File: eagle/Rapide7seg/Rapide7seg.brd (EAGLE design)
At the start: 50 x 50 mm, 47 parts, among them IC1 MEGA8-P, J1 AVR_SPI_PRG_6PTH

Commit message: First version, sent to production
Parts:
- moved C3 0.90 mm to (1.91, 40.0), turned to 270 degrees
- moved LED4 0.64 mm to (40.0, 43.2)
- moved LED1 0.63 mm to (9.53, 43.2)
- moved H1 0.63 mm to (47.6, 47.0)
- moved LED2 0.63 mm to (19.7, 43.2)
- moved LED3 0.63 mm to (29.8, 43.2)
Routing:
- net UCRESET: track 0.00 -> 126.0 mm, vias 0 -> 3
- net GND: track 0.00 -> 125.9 mm, vias 0 -> 2
- net VCC: track 0.00 -> 114.2 mm, vias 0 -> 2
- net N$21: track 0.00 -> 86.4 mm, vias 0 -> 4
- net N$23: track 0.00 -> 86.3 mm, vias 0 -> 2
- net N$16: track 0.00 -> 63.2 mm, vias 0 -> 2
- net N$19: track 0.00 -> 61.6 mm, vias 0 -> 4
- net N$17: track 0.00 -> 60.3 mm, vias 0 -> 2
- net N$1: track 0.00 -> 59.8 mm
- net N$9: track 0.00 -> 55.0 mm
- net N$11: track 0.00 -> 50.0 mm
- net L3: track 0.00 -> 49.5 mm, vias 0 -> 2
- net N$26: track 0.00 -> 48.8 mm, vias 0 -> 1
- net L1: track 0.00 -> 48.4 mm, vias 0 -> 2
- net N$22: track 0.00 -> 48.0 mm, vias 0 -> 3
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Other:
- board text removed: "Order #######"

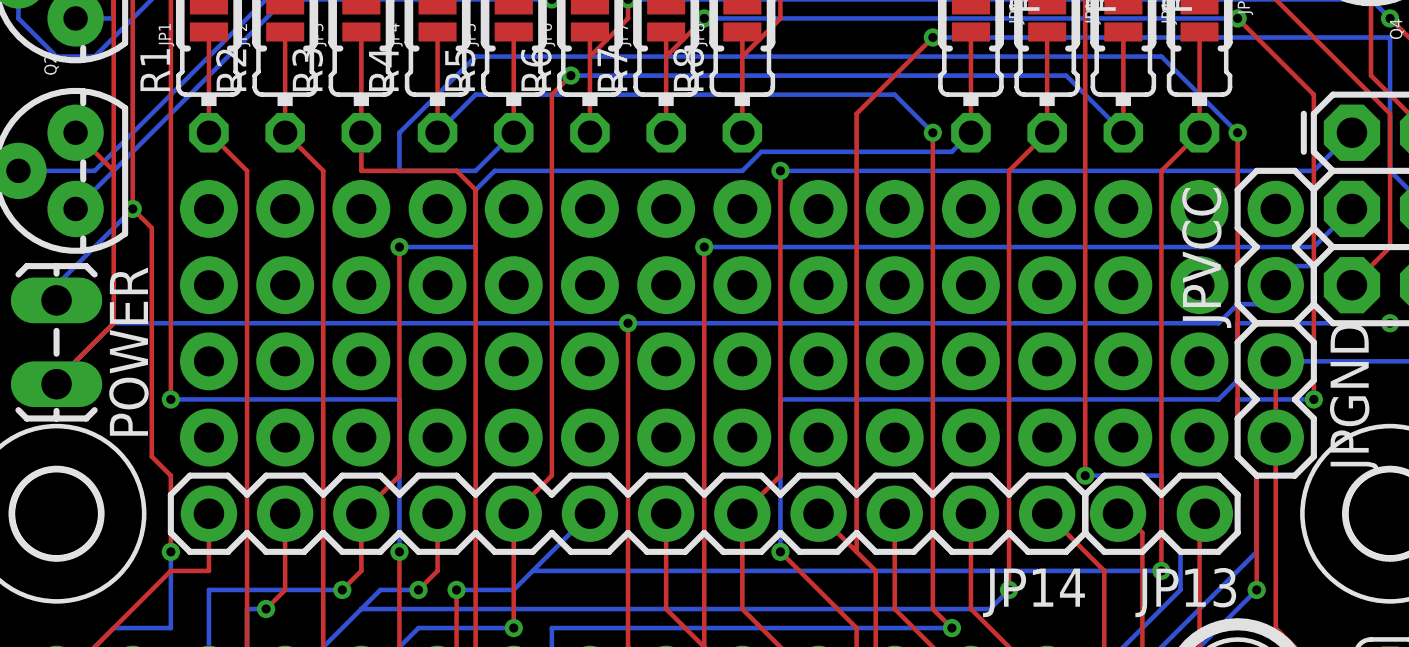
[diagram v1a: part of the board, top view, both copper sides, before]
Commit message: edit/bugfix (wrongly used vias instead of pins)
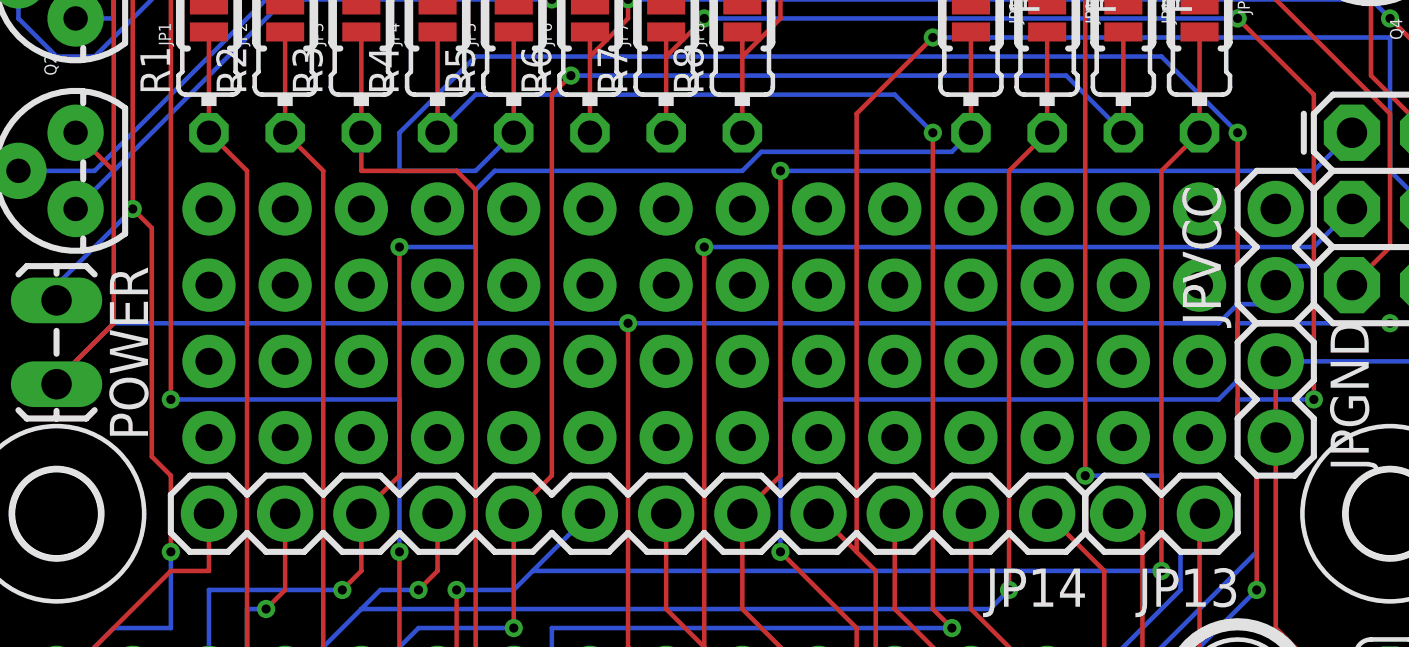
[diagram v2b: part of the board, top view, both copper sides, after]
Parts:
- added U$1, U$2, U$3, U$4, U$5, U$6, U$7, U$8: M7_NOSILK, kalshagar:M7_NOSILK
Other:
- board text added: "v1.1 Mar2013"
- board text removed: "v1.0 Nov2012"
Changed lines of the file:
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@@
 <layer number="144" name="Drill_legend" color="7" fill="1" visible="no" active="yes"/>
 <layer number="151" name="HeatSink" color="7" fill="1" visible="no" active="yes"/>
+<layer number="199" name="Contour" color="7" fill="1" visible="yes" active="yes"/>
 <layer number="200" name="200bmp" color="1" fill="10" visible="no" active="yes"/>
 <layer number="201" name="201bmp" color="2" fill="10" visible="no" active="yes"/>
@@
 <text x="24.13" y="6.35" size="1.4224" layer="125">Rapide7seg</text>
 <text x="6.35" y="3.81" size="1.016" layer="125">kalshagar.wikispaces.com/Rapide7seg</text>
-<text x="27.94" y="5.08" size="0.8128" layer="125">v1.0 Nov2012</text>
+<text x="27.94" y="5.08" size="0.8128" layer="125">v1.1 Mar2013</text>
 <wire x1="46.355" y1="17.78" x2="46.355" y2="20.32" width="0.254" layer="125"/>
 <wire x1="46.355" y1="20.32" x2="44.45" y2="20.32" width="0.254" layer="125"/>
@@
 <element name="JPVCC" library="SparkFun" package="1X02" value="" x="43.18" y="22.86" rot="R90"/>
 <element name="C3" library="resistor" package="E1,8-4" value="" x="1.905" y="40.005" rot="R270"/>
+<element name="U$1" library="kalshagar" package="M7_NOSILK" value="M7_NOSILK" x="7.62" y="17.78"/>
+<element name="U$2" library="kalshagar" package="M7_NOSILK" value="M7_NOSILK" x="25.4" y="17.78"/>
+<element name="U$3" library="kalshagar" package="M7_NOSILK" value="M7_NOSILK" x="7.62" y="20.32"/>
+<element name="U$4" library="kalshagar" package="M7_NOSILK" value="M7_NOSILK" x="25.4" y="20.32"/>
+<element name="U$5" library="kalshagar" package="M7_NOSILK" value="M7_NOSILK" x="7.62" y="22.86"/>
+<element name="U$6" library="kalshagar" package="M7_NOSILK" value="M7_NOSILK" x="25.4" y="22.86"/>
+<element name="U$7" library="kalshagar" package="M7_NOSILK" value="M7_NOSILK" x="7.62" y="25.4"/>
+<element name="U$8" library="kalshagar" package="M7_NOSILK" value="M7_NOSILK" x="25.4" y="25.4"/>
 </elements>
 <signals>
@@
 <wire x1="35.56" y1="15.24" x2="37.465" y2="13.335" width="0.1524" layer="1"/>
 </signal>
-<signal name="N$43">
-<via x="7.62" y="25.4" extent="1-16" drill="1" diameter="1.9304"/>
-</signal>
-<signal name="N$44">
-<via x="7.62" y="22.86" extent="1-16" drill="1" diameter="1.9304"/>
-</signal>
-<signal name="N$45">
-<via x="7.62" y="17.78" extent="1-16" drill="1" diameter="1.9304"/>
-</signal>
-<signal name="N$42">
-<via x="7.62" y="20.32" extent="1-16" drill="1" diameter="1.9304"/>
-</signal>
-<signal name="N$46">
-<via x="10.16" y="25.4" extent="1-16" drill="1" diameter="1.9304"/>
-</signal>
-<signal name="N$47">
-<via x="10.16" y="22.86" extent="1-16" drill="1" diameter="1.9304"/>
-</signal>
-<signal name="N$48">
-<via x="10.16" y="17.78" extent="1-16" drill="1" diameter="1.9304"/>
-</signal>
-<signal name="N$35">
-<via x="10.16" y="20.32" extent="1-16" drill="1" diameter="1.9304"/>
-</signal>
-<signal name="N$53">
-<via x="12.7" y="22.86" extent="1-16" drill="1" diameter="1.9304"/>
-</signal>
-<signal name="N$54">
-<via x="12.7" y="17.78" extent="1-16" drill="1" diameter="1.9304"/>
-</signal>
-<signal name="N$49">
-<via x="12.7" y="20.32" extent="1-16" drill="1" diameter="1.9304"/>
-</signal>
-<signal name="N$50">
-<via x="12.7" y="25.4" extent="1-16" drill="1" diameter="1.9304"/>
-</signal>
-<signal name="N$51">
-<via x="15.24" y="25.4" extent="1-16" drill="1" diameter="1.9304"/>
-</signal>
-<signal name="N$52">
-<via x="15.24" y="22.86" extent="1-16" drill="1" diameter="1.9304"/>
-</signal>
-<signal name="N$55">
-<via x="15.24" y="17.78" extent="1-16" drill="1" diameter="1.9304"/>
-</signal>
-<signal name="N$36">
-<via x="15.24" y="20.32" extent="1-16" drill="1" diameter="1.9304"/>
-</signal>
-<signal name="N$57">
-<via x="17.78" y="25.4" extent="1-16" drill="1" diameter="1.9304"/>
-</signal>
-<signal name="N$60">
-<via x="17.78" y="22.86" extent="1-16" drill="1" diameter="1.9304"/>
-</signal>
-<signal name="N$61">
-<via x="17.78" y="17.78" extent="1-16" drill="1" diameter="1.9304"/>
-</signal>
-<signal name="N$56">
-<via x="17.78" y="20.32" extent="1-16" drill="1" diameter="1.9304"/>
-</signal>
-<signal name="N$58">
-<via x="20.32" y="25.4" extent="1-16" drill="1" diameter="1.9304"/>
-</signal>
-<signal name="N$59">
-<via x="20.32" y="22.86" extent="1-16" drill="1" diameter="1.9304"/>
-</signal>
-<signal name="N$62">
-<via x="20.32" y="17.78" extent="1-16" drill="1" diameter="1.9304"/>
-</signal>
-<signal name="N$37">
-<via x="20.32" y="20.32" extent="1-16" drill="1" diameter="1.9304"/>
-</signal>
-<signal name="N$65">
-<via x="22.86" y="25.4" extent="1-16" drill="1" diameter="1.9304"/>
-</signal>
-<signal name="N$66">
-<via x="22.86" y="22.86" extent="1-16" drill="1" diameter="1.9304"/>
-</signal>
-<signal name="N$69">
-<via x="22.86" y="17.78" extent="1-16" drill="1" diameter="1.9304"/>
-</signal>
-<signal name="N$63">
-<via x="22.86" y="20.32" extent="1-16" drill="1" diameter="1.9304"/>
-</signal>
-<signal name="N$64">
-<via x="25.4" y="25.4" extent="1-16" drill="1" diameter="1.9304"/>
-</signal>
-<signal name="N$67">
-<via x="25.4" y="22.86" extent="1-16" drill="1" diameter="1.9304"/>
-</signal>
-<signal name="N$68">
-<via x="25.4" y="17.78" extent="1-16" drill="1" diameter="1.9304"/>
-</signal>
-<signal name="N$38">
-<via x="25.4" y="20.32" extent="1-16" drill="1" diameter="1.9304"/>
-</signal>
-<signal name="N$74">
-<via x="27.94" y="22.86" extent="1-16" drill="1" diameter="1.9304"/>
-</signal>
-<signal name="N$75">
-<via x="27.94" y="17.78" extent="1-16" drill="1" diameter="1.9304"/>
-</signal>
-<signal name="N$70">
-<via x="27.94" y="20.32" extent="1-16" drill="1" diameter="1.9304"/>
-</signal>
-<signal name="N$71">
-<via x="27.94" y="25.4" extent="1-16" drill="1" diameter="1.9304"/>
-</signal>
-<signal name="N$72">
-<via x="30.48" y="25.4" extent="1-16" drill="1" diameter="1.9304"/>
-</signal>
-<signal name="N$73">
-<via x="30.48" y="22.86" extent="1-16" drill="1" diameter="1.9304"/>
-</signal>
-<signal name="N$76">
-<via x="30.48" y="17.78" extent="1-16" drill="1" diameter="1.9304"/>
-</signal>
-<signal name="N$39">
-<via x="30.48" y="20.32" extent="1-16" drill="1" diameter="1.9304"/>
-</signal>
-<signal name="N$78">
-<via x="33.02" y="25.4" extent="1-16" drill="1" diameter="1.9304"/>
-</signal>
-<signal name="N$81">
-<via x="33.02" y="22.86" extent="1-16" drill="1" diameter="1.9304"/>
-</signal>
-<signal name="N$82">
-<via x="33.02" y="17.78" extent="1-16" drill="1" diameter="1.9304"/>
-</signal>
-<signal name="N$77">
-<via x="33.02" y="20.32" extent="1-16" drill="1" diameter="1.9304"/>
-</signal>
-<signal name="N$79">
-<via x="35.56" y="25.4" extent="1-16" drill="1" diameter="1.9304"/>
-</signal>
-<signal name="N$80">
-<via x="35.56" y="22.86" extent="1-16" drill="1" diameter="1.9304"/>
-</signal>
-<signal name="N$83">
-<via x="35.56" y="17.78" extent="1-16" drill="1" diameter="1.9304"/>
-</signal>
-<signal name="N$40">
-<via x="35.56" y="20.32" extent="1-16" drill="1" diameter="1.9304"/>
-</signal>
-<signal name="N$86">
-<via x="38.1" y="25.4" extent="1-16" drill="1" diameter="1.9304"/>
-</signal>
-<signal name="N$87">
-<via x="38.1" y="22.86" extent="1-16" drill="1" diameter="1.9304"/>
-</signal>
-<signal name="N$90">
-<via x="38.1" y="17.78" extent="1-16" drill="1" diameter="1.9304"/>
-</signal>
-<signal name="N$84">
-<via x="38.1" y="20.32" extent="1-16" drill="1" diameter="1.9304"/>
-</signal>
-<signal name="N$85">
-<via x="40.64" y="25.4" extent="1-16" drill="1" diameter="1.9304"/>
-</signal>
-<signal name="N$88">
-<via x="40.64" y="22.86" extent="1-16" drill="1" diameter="1.9304"/>
-</signal>
-<signal name="N$89">
-<via x="40.64" y="17.78" extent="1-16" drill="1" diameter="1.9304"/>
-</signal>
-<signal name="N$41">
-<via x="40.64" y="20.32" extent="1-16" drill="1" diameter="1.9304"/>
-</signal>
 </signals>
